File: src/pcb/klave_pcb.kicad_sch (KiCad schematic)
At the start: 54 parts, among them J1 TRRS, SW1 0:0, SW10 1:3, SW11 1:4, SW12 1:5, SW13 2:0, SW14 2:1, SW15 2:2, SW16 2:3, SW17 2:4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

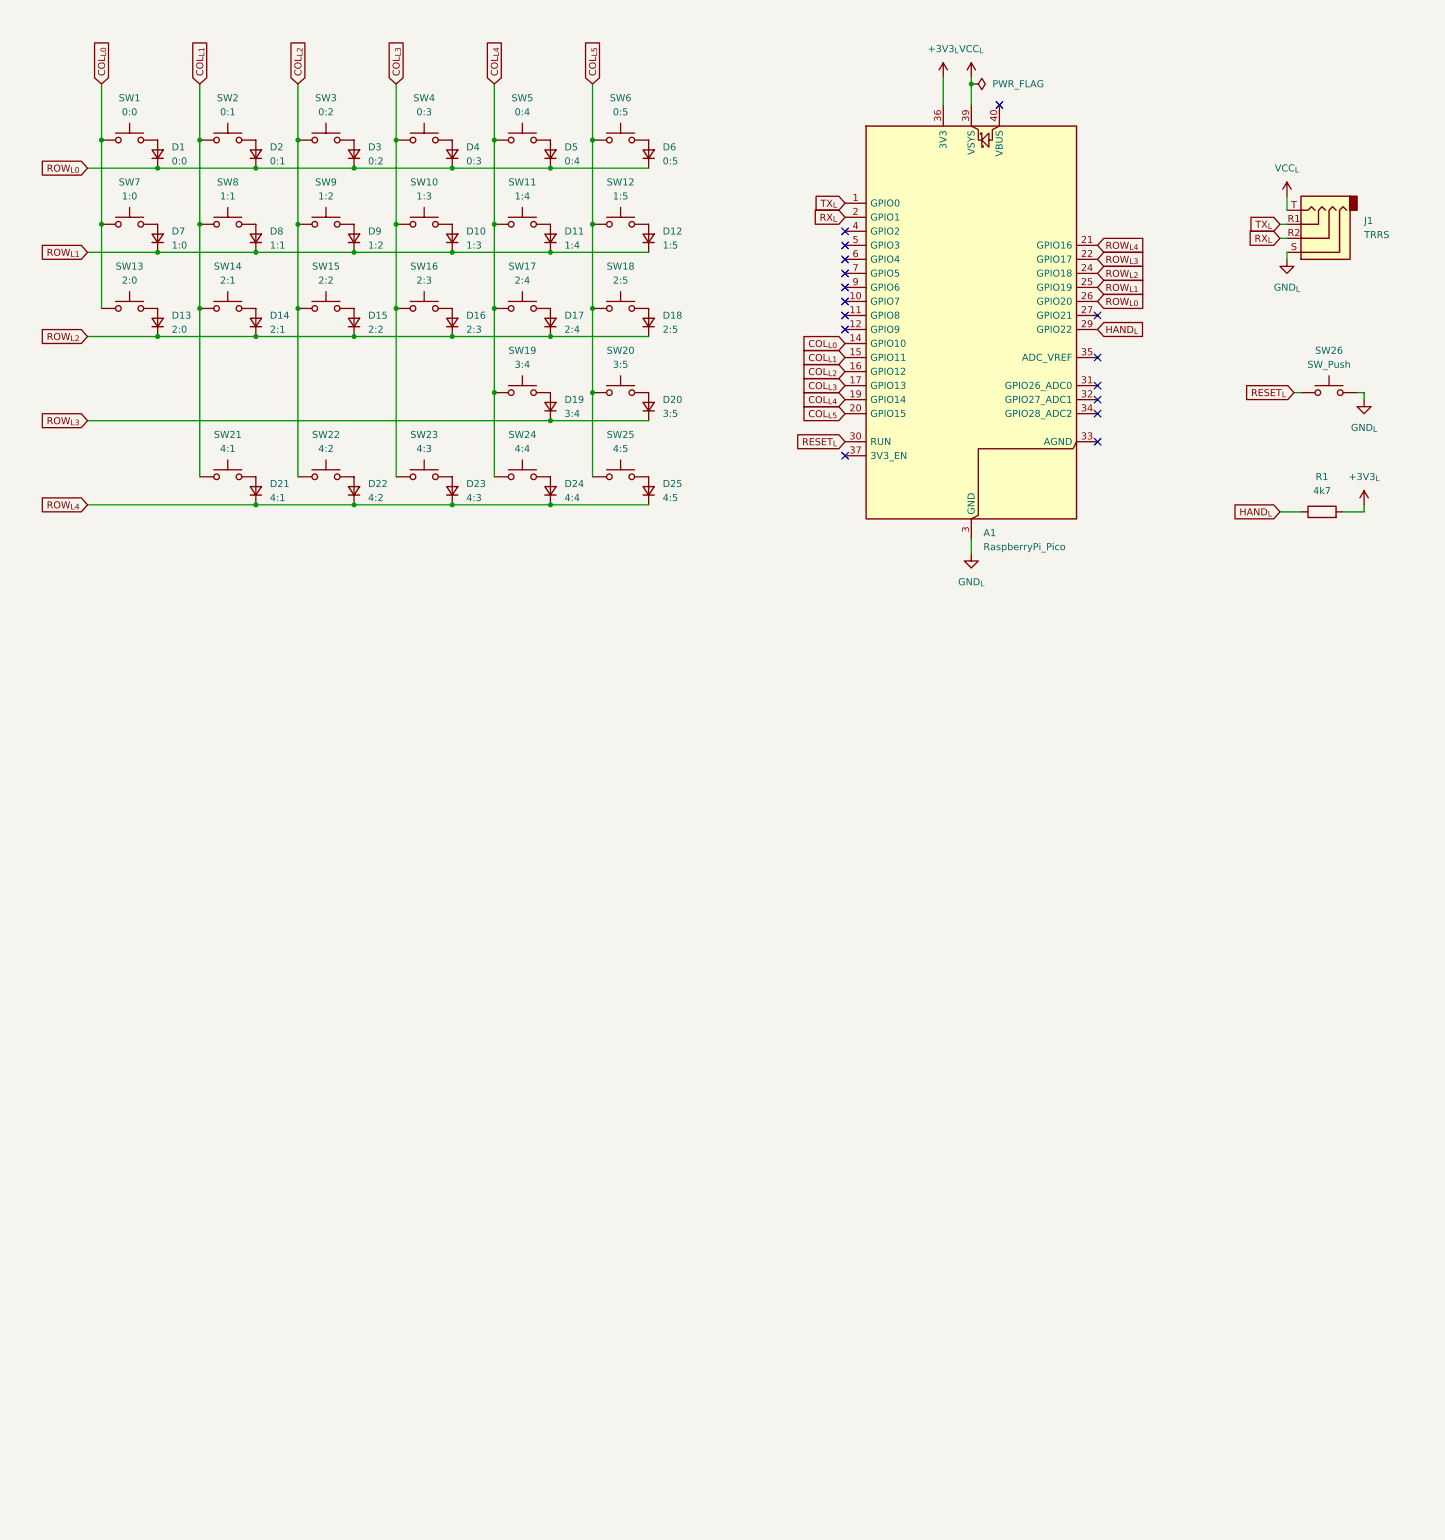
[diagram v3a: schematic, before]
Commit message: Add right half
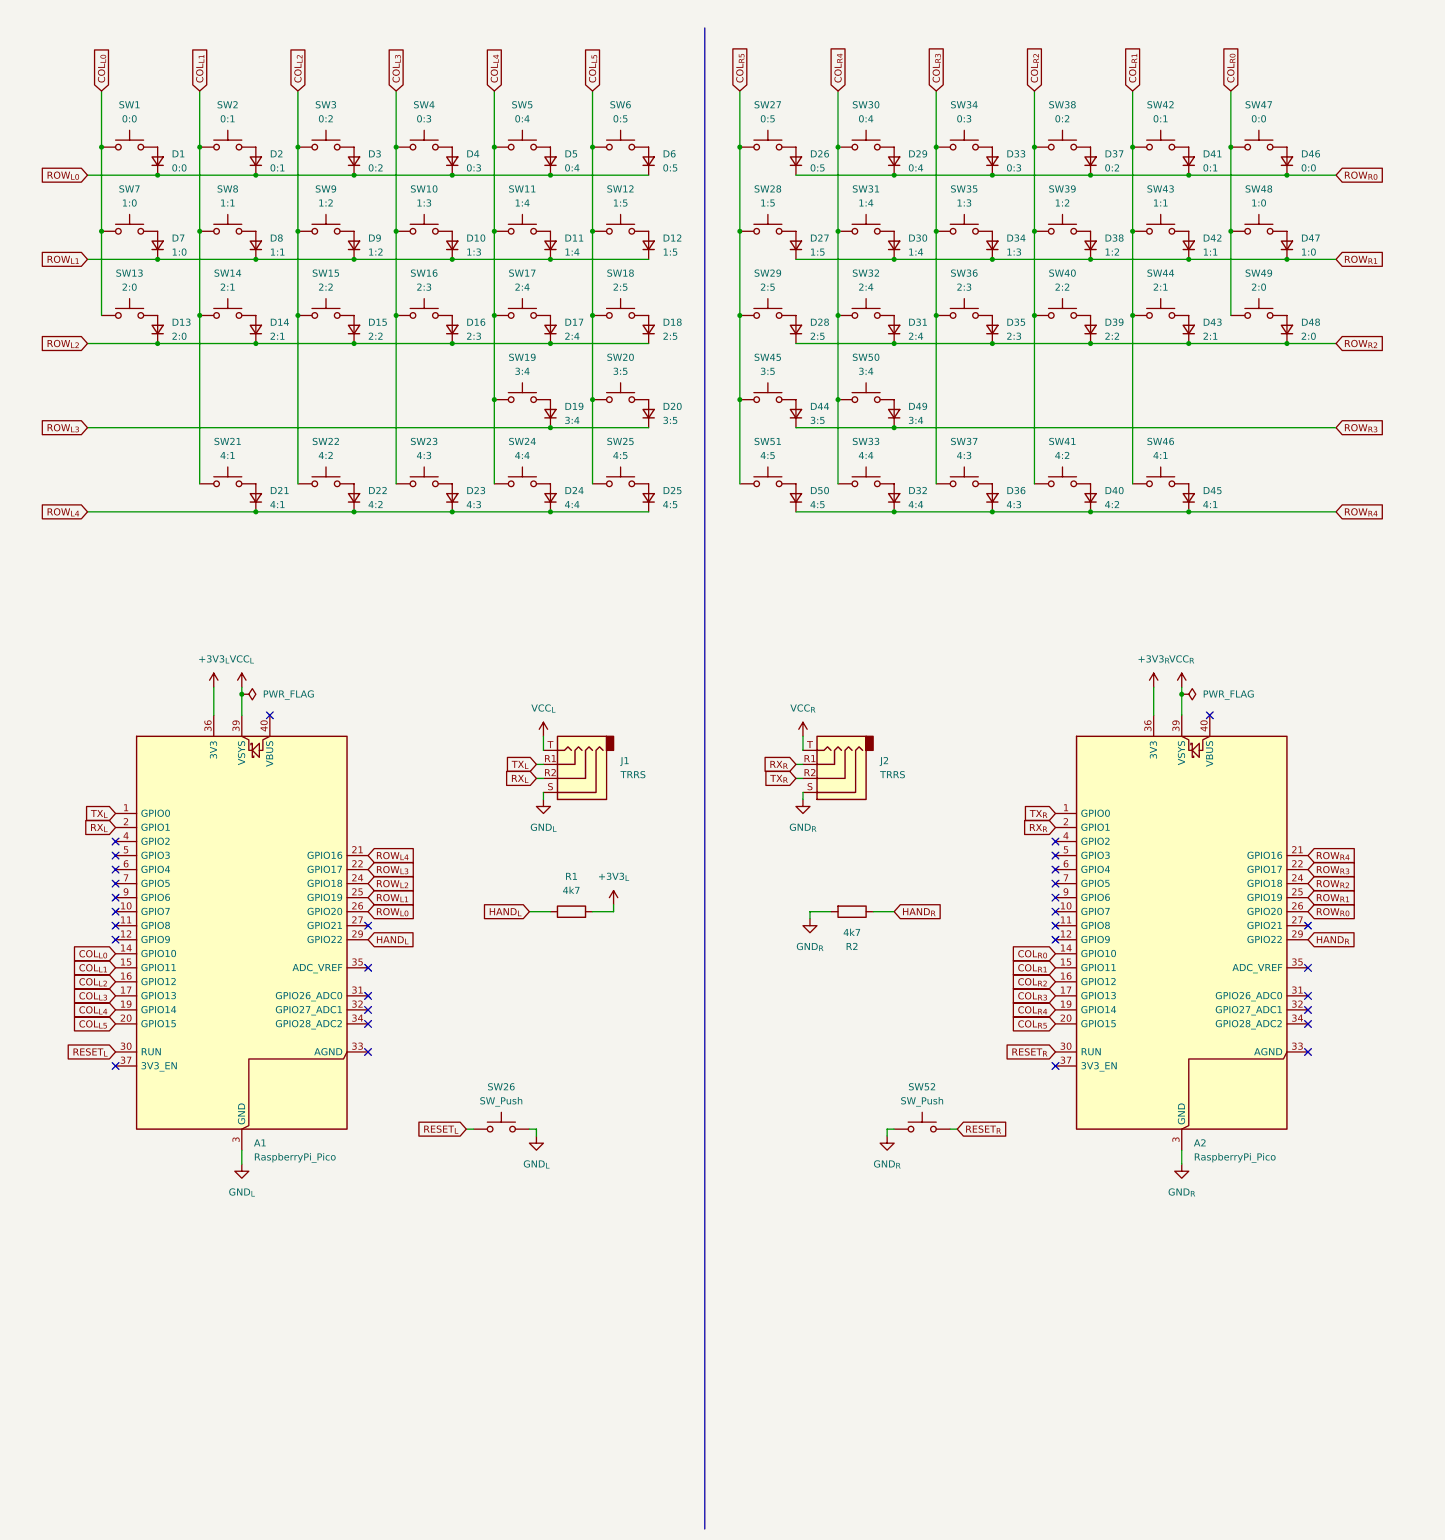
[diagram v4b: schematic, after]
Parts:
- added A2: RaspberryPi_Pico, Module_RaspberryPi_Pico:RaspberryPi_Pico_Common, symbol MCU_Module_RaspberryPi_Pico:RaspberryPi_Pico
- added D26: 0:5, symbol Device:D_Small
- added D27: 1:5, symbol Device:D_Small
- added D28: 2:5, symbol Device:D_Small
- added D29: 0:4, symbol Device:D_Small
- added D30: 1:4, symbol Device:D_Small
- added D31: 2:4, symbol Device:D_Small
- added D32: 4:4, symbol Device:D_Small
- added D33: 0:3, symbol Device:D_Small
- added D34: 1:3, symbol Device:D_Small
- added D35: 2:3, symbol Device:D_Small
- added D36: 4:3, symbol Device:D_Small
- added D37: 0:2, symbol Device:D_Small
- added D38: 1:2, symbol Device:D_Small
- added D39: 2:2, symbol Device:D_Small
- added D40: 4:2, symbol Device:D_Small
- added D41: 0:1, symbol Device:D_Small
- added D42: 1:1, symbol Device:D_Small
- added D43: 2:1, symbol Device:D_Small
- added D44: 3:5, symbol Device:D_Small
- added D45: 4:1, symbol Device:D_Small
- added D46: 0:0, symbol Device:D_Small
- added D47: 1:0, symbol Device:D_Small
- added D48: 2:0, symbol Device:D_Small
- added D49: 3:4, symbol Device:D_Small
- added D50: 4:5, symbol Device:D_Small
- added J2: TRRS, symbol Connector_Audio:AudioJack4
- added R2: 4k7, symbol Device:R
- added SW27: 0:5, symbol Switch:SW_Push
- added SW28: 1:5, symbol Switch:SW_Push
- added SW29: 2:5, symbol Switch:SW_Push
- added SW30: 0:4, symbol Switch:SW_Push
- added SW31: 1:4, symbol Switch:SW_Push
- added SW32: 2:4, symbol Switch:SW_Push
- added SW33: 4:4, symbol Switch:SW_Push
- added SW34: 0:3, symbol Switch:SW_Push
- added SW35: 1:3, symbol Switch:SW_Push
- added SW36: 2:3, symbol Switch:SW_Push
- added SW37: 4:3, symbol Switch:SW_Push
- added SW38: 0:2, symbol Switch:SW_Push
- added SW39: 1:2, symbol Switch:SW_Push
- added SW40: 2:2, symbol Switch:SW_Push
- added SW41: 4:2, symbol Switch:SW_Push
- added SW42: 0:1, symbol Switch:SW_Push
- added SW43: 1:1, symbol Switch:SW_Push
- added SW44: 2:1, symbol Switch:SW_Push
- added SW45: 3:5, symbol Switch:SW_Push
- added SW46: 4:1, symbol Switch:SW_Push
- added SW47: 0:0, symbol Switch:SW_Push
- added SW48: 1:0, symbol Switch:SW_Push
- added SW49: 2:0, symbol Switch:SW_Push
- added SW50: 3:4, symbol Switch:SW_Push
- added SW51: 4:5, symbol Switch:SW_Push
- added SW52: SW_Push, symbol Switch:SW_Push
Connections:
- new net: D50.2 (A), SW51.2
- new net: D40.2 (A), SW41.2
- new net: D35.2 (A), SW36.2
- new net: D30.2 (A), SW31.2
- new net: D26.2 (A), SW27.2
- new net: D46.2 (A), SW47.2
- new net: D39.2 (A), SW40.2
- new net: D27.2 (A), SW28.2
- new net: D43.2 (A), SW44.2
- new net: D32.2 (A), SW33.2
- new net: D34.2 (A), SW35.2
- new net: D44.2 (A), SW45.2
- new net: D49.2 (A), SW50.2
- new net: D29.2 (A), SW30.2
- new net: D41.2 (A), SW42.2
- new net: D45.2 (A), SW46.2
- new net: D36.2 (A), SW37.2
- new net: D33.2 (A), SW34.2
- new net: D47.2 (A), SW48.2
- new net: D48.2 (A), SW49.2
- new net: D37.2 (A), SW38.2
- new net: D38.2 (A), SW39.2
- new net: D42.2 (A), SW43.2
- new net: D28.2 (A), SW29.2
- new net: D31.2 (A), SW32.2
- new net +3V3_{R}: A2.36 (3V3)
- new net COL_{R0}: A2.14 (GPIO10), SW47.1, SW48.1, SW49.1
- new net COL_{R1}: A2.15 (GPIO11), SW42.1, SW43.1, SW44.1, SW46.1
- new net COL_{R2}: A2.16 (GPIO12), SW38.1, SW39.1, SW40.1, SW41.1
- new net COL_{R3}: A2.17 (GPIO13), SW34.1, SW35.1, SW36.1, SW37.1
- new net COL_{R4}: A2.19 (GPIO14), SW30.1, SW31.1, SW32.1, SW33.1, SW50.1
- new net COL_{R5}: A2.20 (GPIO15), SW27.1, SW28.1, SW29.1, SW45.1, SW51.1
- new net GND_{R}: A2.13 (GND), A2.18 (GND), A2.23 (GND), A2.28 (GND), A2.3 (GND), A2.38 (GND), A2.8 (GND), J2.S, R2.2, SW52.1
- new net HAND_{R}: A2.29 (GPIO22), R2.1
- new net RESET_{R}: A2.30 (RUN), SW52.2
- new net ROW_{R0}: A2.26 (GPIO20), D26.1 (K), D29.1 (K), D33.1 (K), D37.1 (K), D41.1 (K), D46.1 (K)
- new net ROW_{R1}: A2.25 (GPIO19), D27.1 (K), D30.1 (K), D34.1 (K), D38.1 (K), D42.1 (K), D47.1 (K)
- new net ROW_{R2}: A2.24 (GPIO18), D28.1 (K), D31.1 (K), D35.1 (K), D39.1 (K), D43.1 (K), D48.1 (K)
- new net ROW_{R3}: A2.22 (GPIO17), D44.1 (K), D49.1 (K)
- new net ROW_{R4}: A2.21 (GPIO16), D32.1 (K), D36.1 (K), D40.1 (K), D45.1 (K), D50.1 (K)
- new net RX_{R}: A2.2 (GPIO1), J2.R1
- new net TX_{R}: A2.1 (GPIO0), J2.R2
- new net VCC_{R}: A2.39 (VSYS), J2.T
- no-connect marks 16 -> 32
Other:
- moved on the sheet: A1, D1, D10, D11, D12, D13, D14, D15, D16, D17, D18, D19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

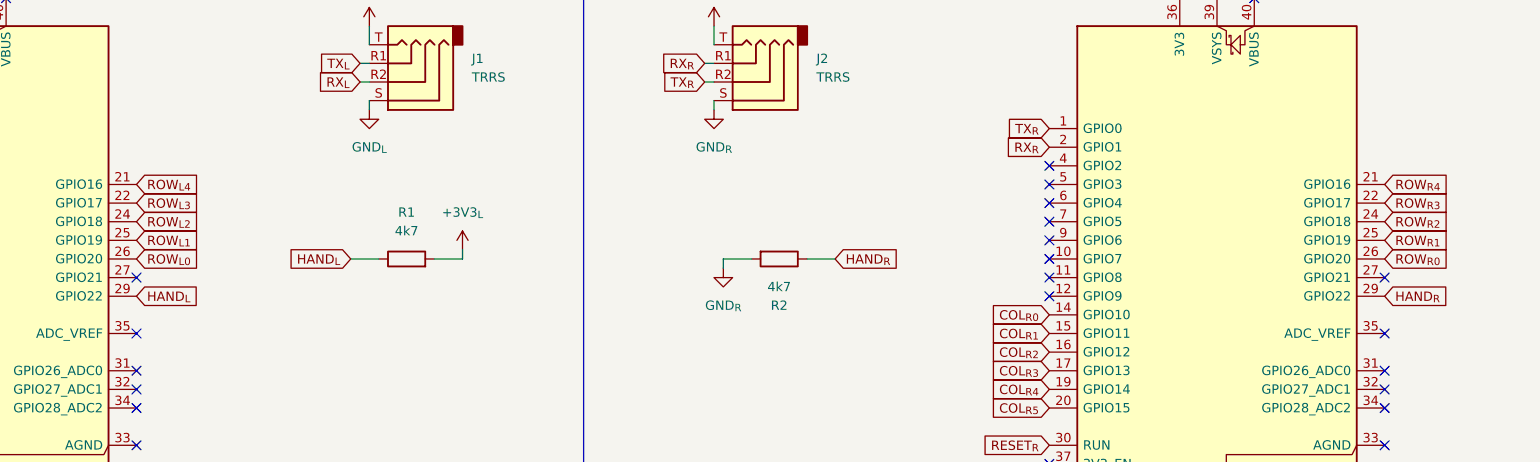
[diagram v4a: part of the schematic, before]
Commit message: Shift rows by one pin
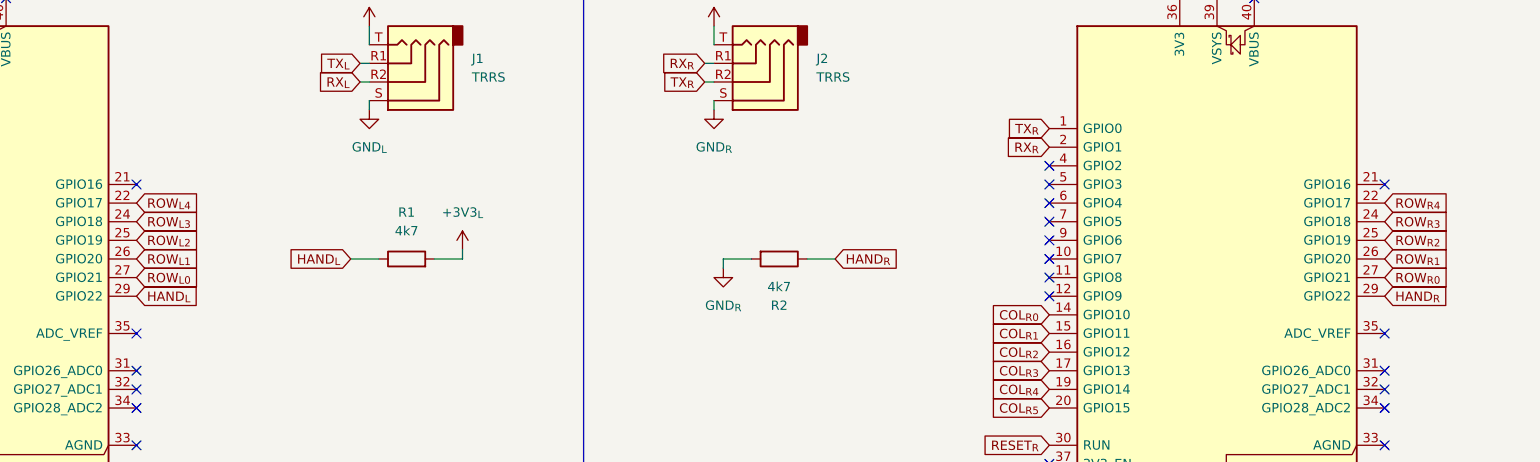
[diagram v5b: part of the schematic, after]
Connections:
- net ROW_{L0}: now also A1.27 (GPIO21); no longer A1.26 (GPIO20)
- net ROW_{L1}: now also A1.26 (GPIO20); no longer A1.25 (GPIO19)
- net ROW_{L2}: now also A1.25 (GPIO19); no longer A1.24 (GPIO18)
- net ROW_{L3}: now also A1.24 (GPIO18); no longer A1.22 (GPIO17)
- net ROW_{L4}: now also A1.22 (GPIO17); no longer A1.21 (GPIO16)
- net ROW_{R0}: now also A2.27 (GPIO21); no longer A2.26 (GPIO20)
- net ROW_{R1}: now also A2.26 (GPIO20); no longer A2.25 (GPIO19)
- net ROW_{R2}: now also A2.25 (GPIO19); no longer A2.24 (GPIO18)
- net ROW_{R3}: now also A2.24 (GPIO18); no longer A2.22 (GPIO17)
- net ROW_{R4}: now also A2.22 (GPIO17); no longer A2.21 (GPIO16)
